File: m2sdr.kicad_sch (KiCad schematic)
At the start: 55 parts, among them J1 Bus_M.2_Socket_B, J2 SMA, J3 SMA, P1 CONN_01X04, P2 CONN_01X01, P3 CONN_01X01, P4 CONN_01X01, P5 CONN_01X01, P6 CONN_01X01, P7 CONN_01X01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

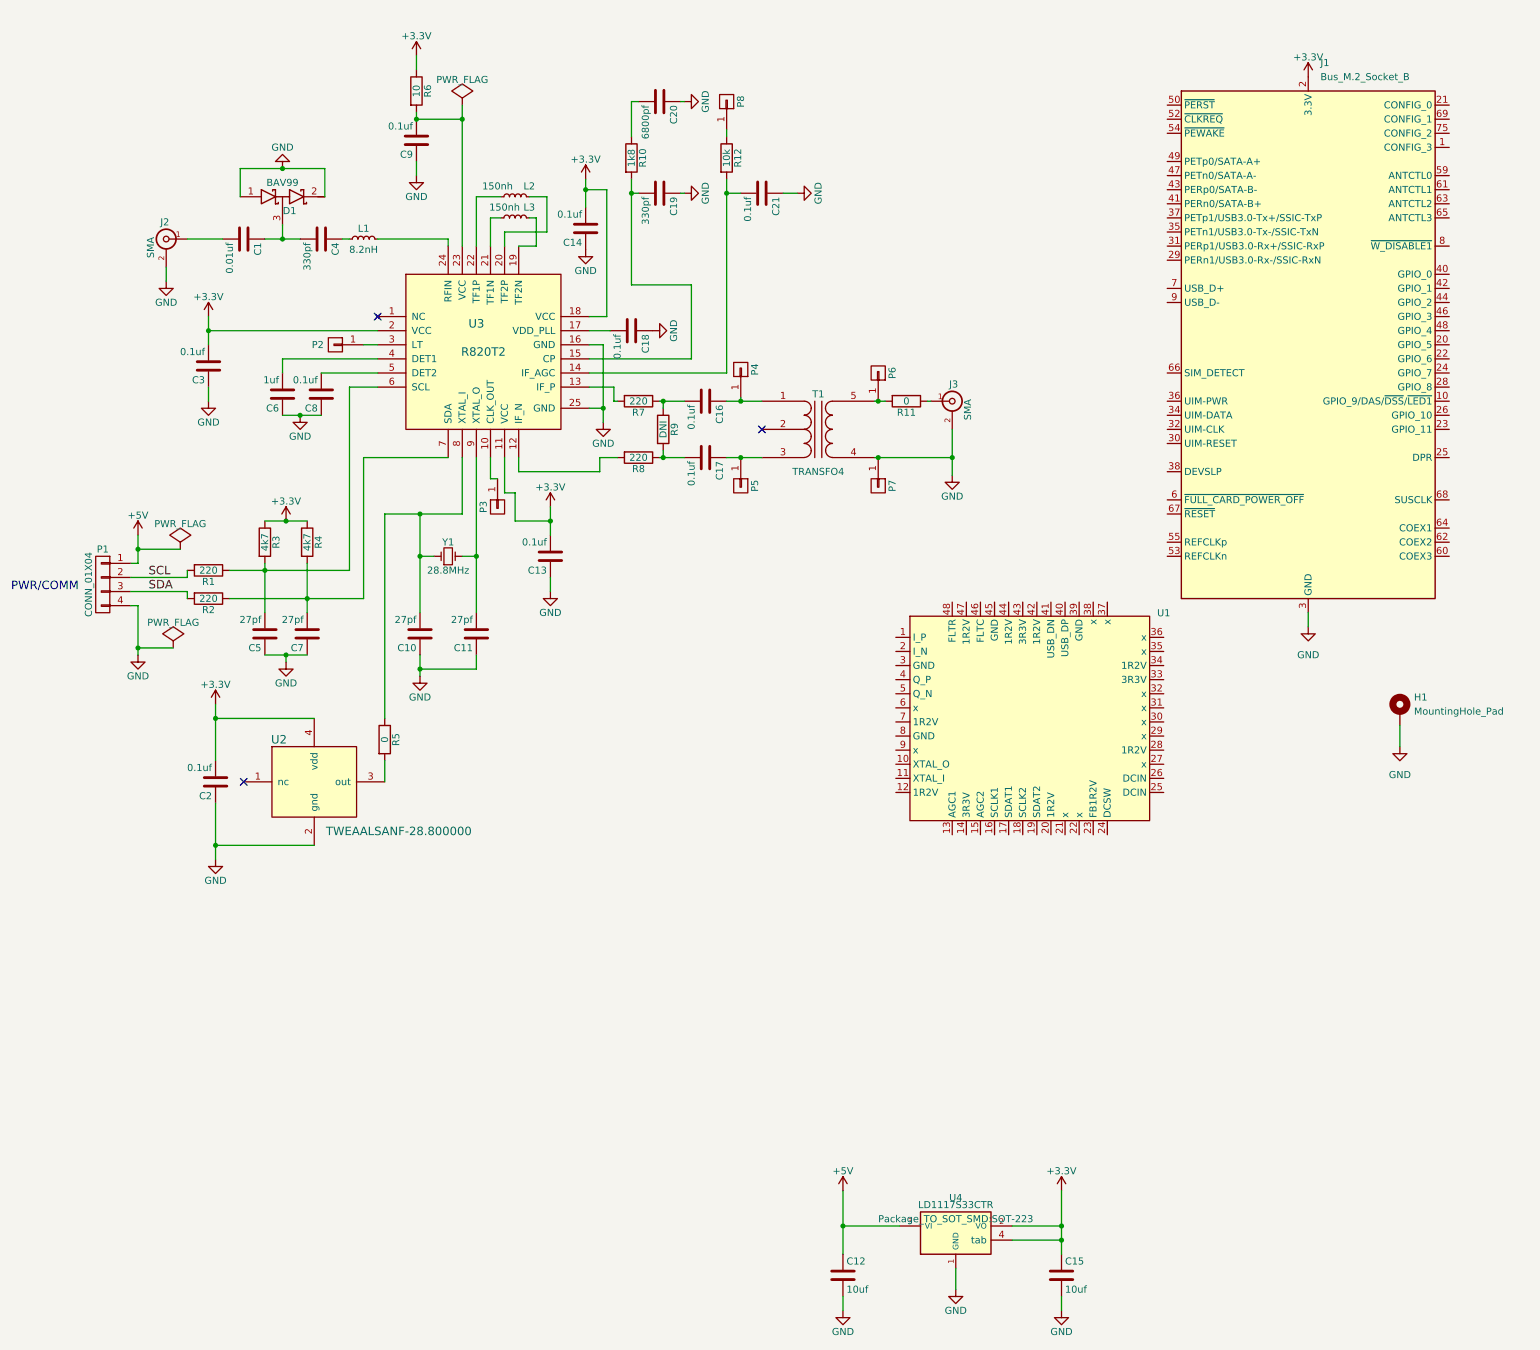
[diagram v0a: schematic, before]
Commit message: Updated m2sdr.kicad_sch
added some rtl2832u components
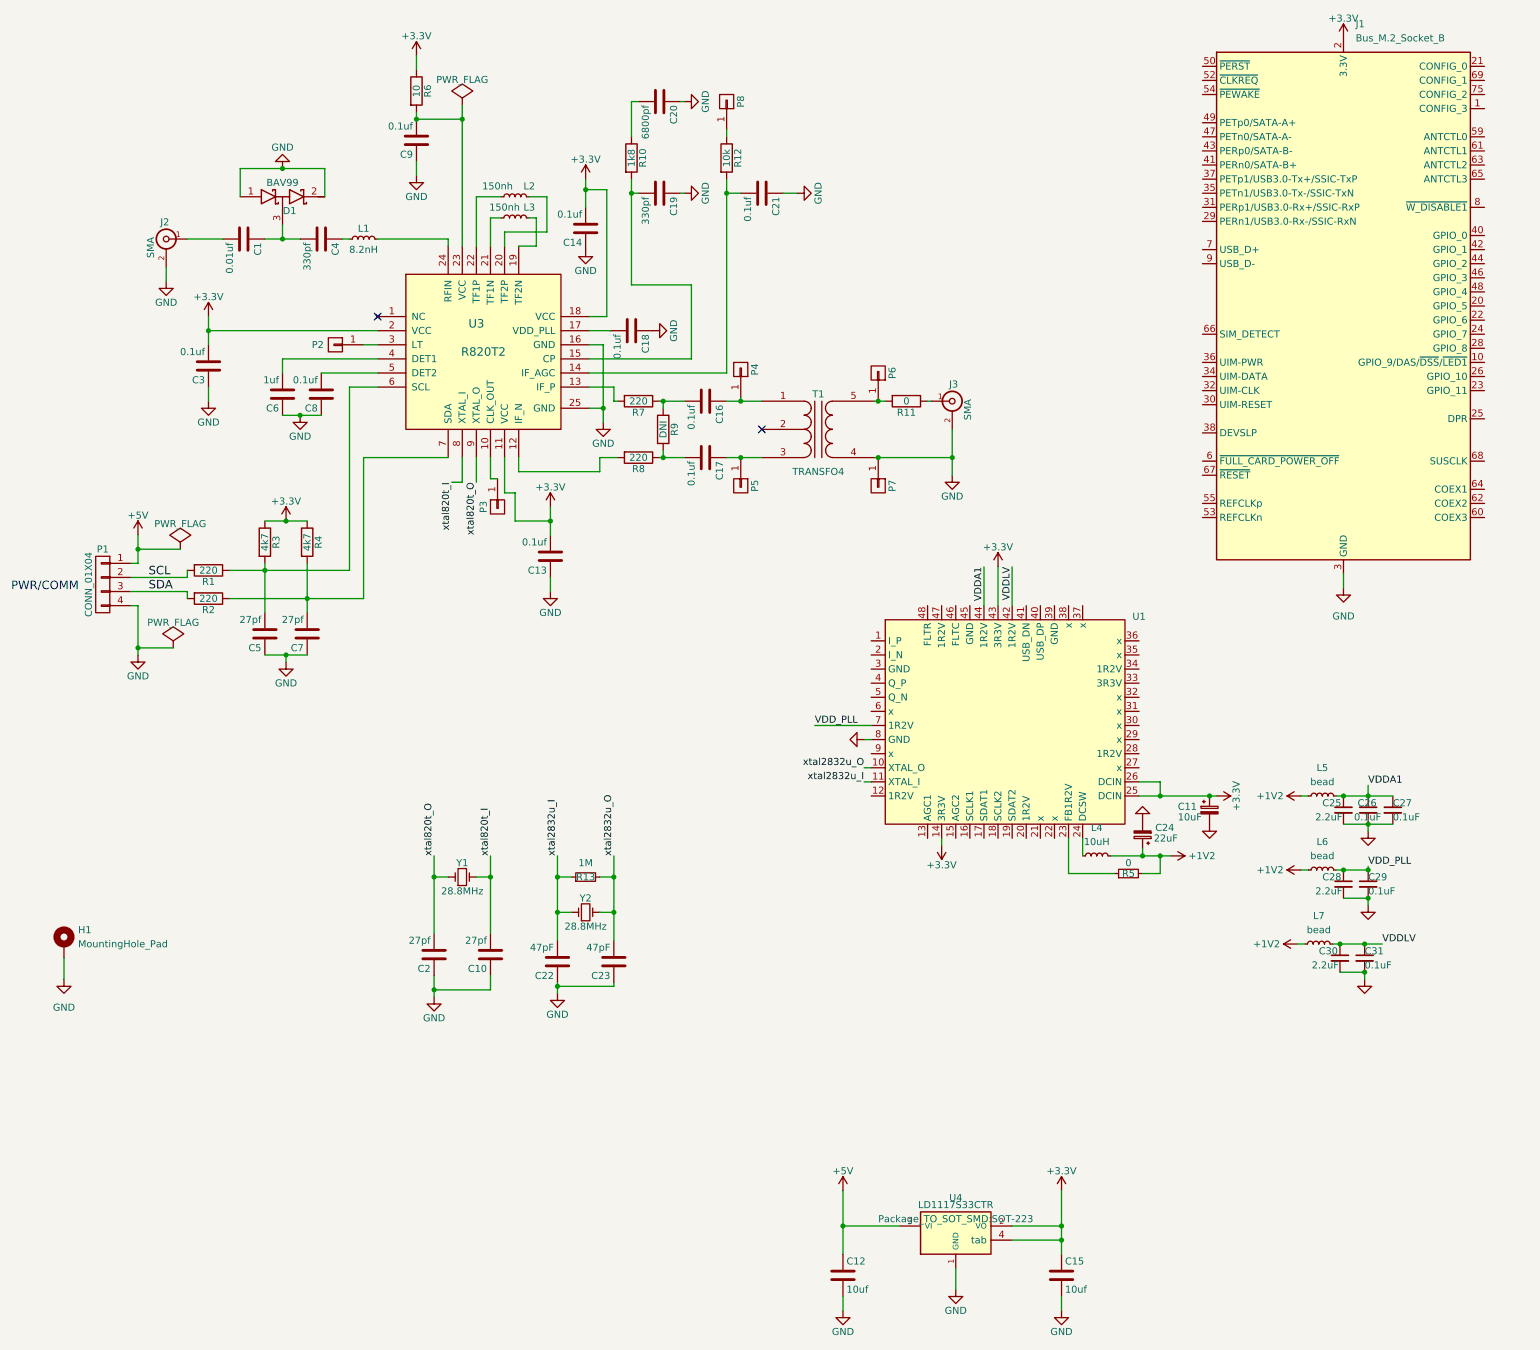
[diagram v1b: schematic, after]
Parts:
- removed C11: 27pf, Capacitor_SMD:C_0603_1608Metric, symbol r820t2_breakout-rescue:C
- removed R5: 0, Resistor_SMD:R_0603_1608Metric, symbol r820t2_breakout-rescue:R
- removed U2: TWEAALSANF-28.800000, Crystal:Crystal_SMD_Abracon_ABM3C-4Pin_5.0x3.2mm, symbol r820t2_breakout-rescue:TCXO
- added C11: 10uF, symbol Device:C_Polarized_Small
- added C22, C23: 47pF, Capacitor_SMD:C_0603_1608Metric, symbol r820t2_breakout-rescue:C
- added C24: 22uF, symbol Device:C_Polarized_Small
- added C25, C28, C30: 2.2uF, symbol Device:C_Small
- added C26, C27, C29, C31: 0.1uF, symbol Device:C_Small
- added L4: 10uH, symbol Device:L_Small
- added L5, L6, L7: bead, symbol Device:L_Small
- added R13: 1M, symbol Device:R_Small
- added R5: 0, symbol Device:R_Small
- added Y2: 28.8MHz, Crystal:Crystal_SMD_HC49-SD, symbol r820t2_breakout-rescue:Crystal_Small
- C2: value 0.1uf -> 27pf
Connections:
- net +3V3: now also U1.14 (3R3V), U1.25 (DCIN), U1.26 (DCIN), U1.43 (3R3V), C11.1; no longer C2.2
- net GND: now also U1.8 (GND), C11.2, C22.1, C23.1, C24.2, C25.2, C26.2, C27.2, C28.2, C29.2, C30.2, C31.2
- net xtal820t_I: now reaches C10.2, U3.8 (XTAL_I)
- net xtal820t_I: now also Y1.2; no longer Y1.1
- net xtal820t_O: now reaches U3.9 (XTAL_O)
- net xtal820t_O: now also C2.2, Y1.1; no longer Y1.2
- net xtal2832u_O: now reaches U1.10 (XTAL_O)
- net xtal2832u_O: now also C23.2, R13.2, Y2.2
- net xtal2832u_I: now reaches U1.11 (XTAL_I)
- net xtal2832u_I: now also C22.2, R13.1, Y2.1
- net at U1.23 (FB1R2V): now also R5.1
- net at U1.24 (DCSW): now also L4.1
- net VDDLV: now reaches U1.42 (1R2V)
- net VDDLV: now also C30.1, C31.1, L7.2
- net VDDA1: now reaches U1.44 (1R2V)
- net VDDA1: now also C25.1, C26.1, C27.1, L5.2
- net VDD_PLL: now reaches U1.7 (1R2V)
- net VDD_PLL: now also C28.1, C29.1, L6.2
- new net +1V2: C24.1, L4.2, L5.1, L6.1, L7.1, R5.2
- no-connect marks 3 -> 2
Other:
- moved on the sheet: H1, J1, U1

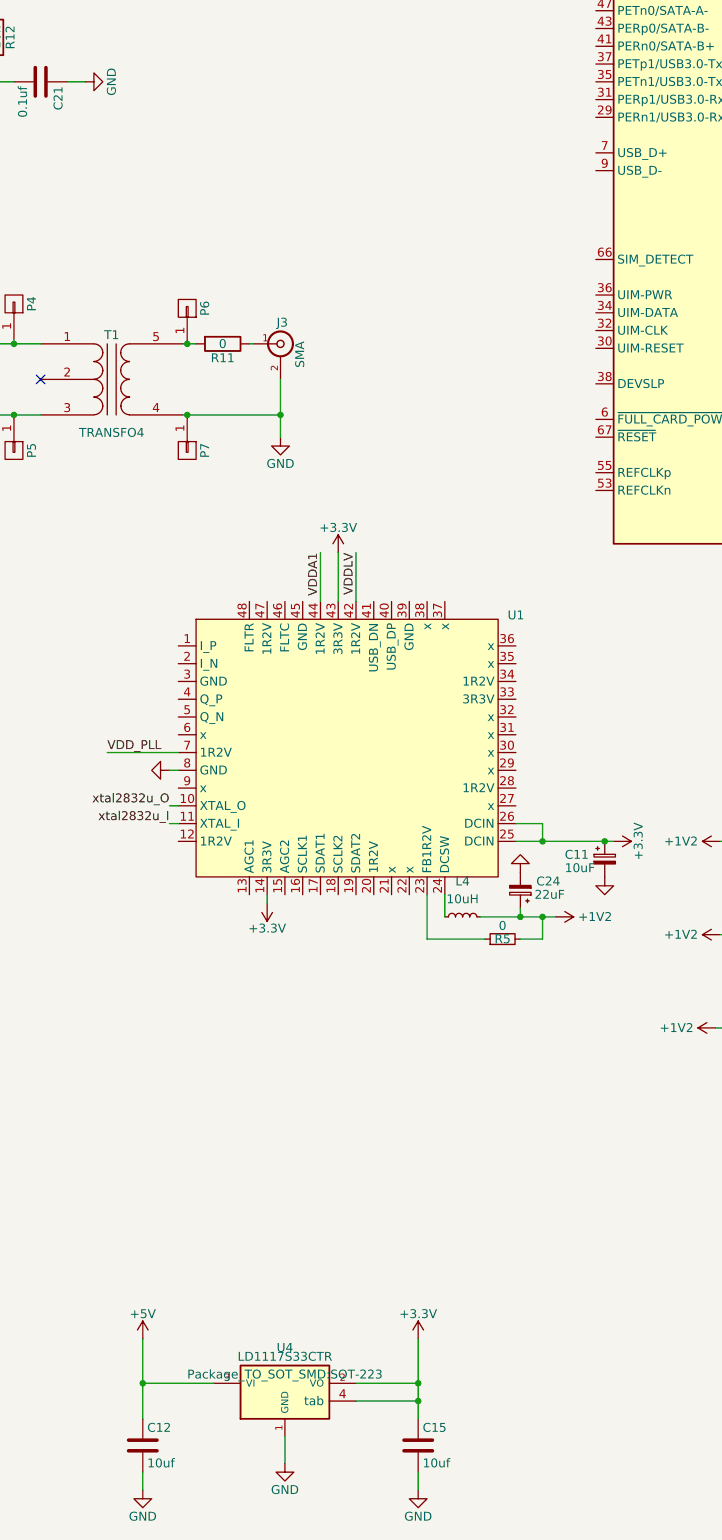
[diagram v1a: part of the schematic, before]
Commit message: Update m2sdr.kicad_sch
removed 5v to 3.3v reg, updated schematic
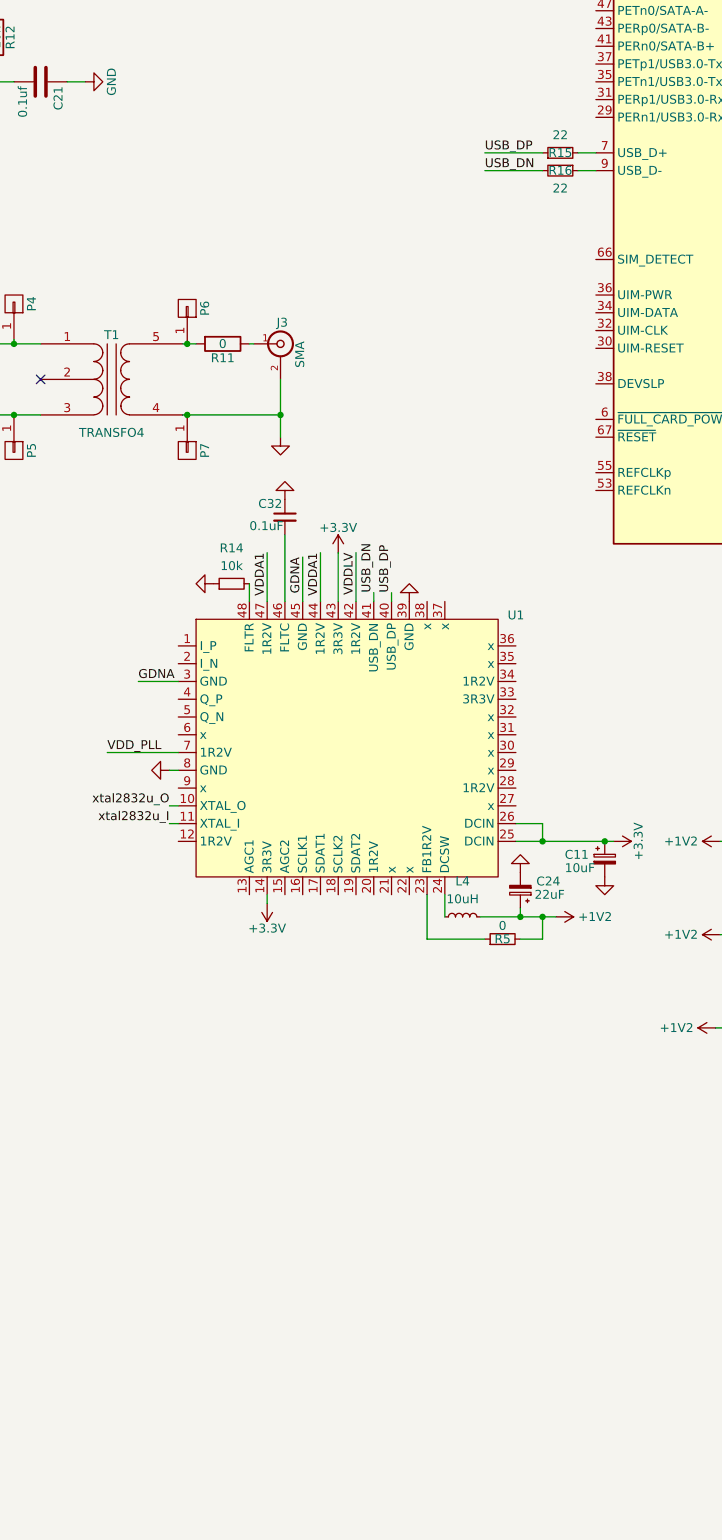
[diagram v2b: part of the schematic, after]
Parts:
- removed C12, C15: 10uf, Capacitor_SMD:C_0805_2012Metric, symbol r820t2_breakout-rescue:C
- removed U4: LD1117S33CTR, Package_TO_SOT_SMD:SOT-223, symbol r820t2_breakout-rescue:LD1117_tab
- added C32: 0.1uF, symbol Device:C_Small
- added R14: 10k, symbol Device:R_Small
- added R15, R16: 22, symbol Device:R_Small
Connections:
- net GND: now also U1.39 (GND), C32.1, R14.1
- net VDDA1: now also U1.47 (1R2V)
- net at J1.7 (USB_D+): now also R15.2
- net at J1.9 (USB_D-): now also R16.1
- net GDNA: now reaches U1.3 (GND)
- net GDNA: now also U1.45 (GND)
- net USB_DP: now reaches U1.40 (USB_DP)
- net USB_DP: now also R15.1
- net USB_DN: now reaches U1.41 (USB_DN)
- net USB_DN: now also R16.2
- net at U1.46 (FLTC): now also C32.2
- net at U1.48 (FLTR): now also R14.2
